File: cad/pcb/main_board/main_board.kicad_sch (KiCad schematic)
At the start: 0 parts

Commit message: VDDA, BOOT SEL
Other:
- sheet MCU ports: added ADC_IN[0..15]; removed none
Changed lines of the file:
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@@
       (effects (font (size 1.27 1.27)) (justify left top))
+    )
+    (pin "ADC_IN[0..15]" input (at 103.505 59.69 0)
+      (effects (font (size 1.27 1.27)) (justify right))
     )
     (instances

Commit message: HSE, usb, TC
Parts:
- added J1: USB_B_Micro, symbol Connector:USB_B_Micro
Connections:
- new net MCU/USB_D+: J1.3 (D+)
- new net MCU/USB_D-: J1.2 (D-)
- new net MCU/USB_ID: J1.4 (ID)
- new net VDD: J1.1 (VBUS)
- new net VSS: J1.5 (GND)
- no-connect marks 0 -> 1
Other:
- added sheet ThermoCouplePins (thermo_couple_pins.kicad_sch)
- sheet MCU ports: added USB_D+, USB_D-, USB_ID; removed none
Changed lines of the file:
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@@
 (kicad_sch (version 20230121) (generator eeschema)
   (paper "A4")
+  (no_connect (at 136.525 60.96))
+  (wire (pts (xy 103.505 66.04) (xy 126.365 66.04))
+    (stroke (width 0) (type default))
+  )
+  (bus (pts (xy 116.84 94.615) (xy 116.84 118.745))
+    (stroke (width 0) (type default))
+  )
+  (wire (pts (xy 103.505 68.58) (xy 126.365 68.58))
+    (stroke (width 0) (type default))
+  )
+  (bus (pts (xy 103.505 94.615) (xy 116.84 94.615))
+    (stroke (width 0) (type default))
+  )
+  (wire (pts (xy 120.65 76.2) (xy 126.365 76.2))
+    (stroke (width 0) (type default))
+  )
+  (wire (pts (xy 103.505 71.12) (xy 126.365 71.12))
+    (stroke (width 0) (type default))
+  )
+  (bus (pts (xy 116.84 118.745) (xy 104.14 118.745))
+    (stroke (width 0) (type default))
+  )
+  (wire (pts (xy 133.985 60.96) (xy 133.985 59.055))
+    (stroke (width 0) (type default))
+  )
+  (wire (pts (xy 120.015 59.055) (xy 133.985 59.055))
+    (stroke (width 0) (type default))
+  )
+  (global_label "VDD" (shape input) (at 120.65 76.2 180) (fields_autoplaced)
+    (effects (font (size 1.27 1.27)) (justify right))
+    (property "Intersheetrefs" "${INTERSHEET_REFS}" (at 114.0362 76.2 0)
+      (effects (font (size 1.27 1.27)) (justify right) hide)
+    )
+  )
+  (global_label "VSS" (shape input) (at 120.015 59.055 180) (fields_autoplaced)
+    (effects (font (size 1.27 1.27)) (justify right))
+    (property "Intersheetrefs" "${INTERSHEET_REFS}" (at 113.5222 59.055 0)
+      (effects (font (size 1.27 1.27)) (justify right) hide)
+    )
+  )
+  (symbol (lib_id "Connector:USB_B_Micro") (at 133.985 71.12 180) (unit 1)
+    (in_bom yes) (on_board yes) (dnp no) (fields_autoplaced)
+    (property "Reference" "J1" (at 140.97 69.85 0)
+      (effects (font (size 1.27 1.27)) (justify right))
+    )
+    (property "Value" "USB_B_Micro" (at 140.97 72.39 0)
+      (effects (font (size 1.27 1.27)) (justify right))
+    )
+    (property "Footprint" "" (at 130.175 69.85 0)
+      (effects (font (size 1.27 1.27)) hide)
+    )
+    (property "Datasheet" "~" (at 130.175 69.85 0)
+      (effects (font (size 1.27 1.27)) hide)
+    )
+    (pin "1")
+    (pin "2")
+    (pin "3")
+    (pin "4")
+    (pin "5")
+    (pin "6")
+    (instances
+      (project "main_board"
+        (path "/6c1b8035-64fa-4797-a506-5c9583cb241c"
+          (reference "J1") (unit 1)
+        )
+      )
+    )
+  )
   (sheet (at 30.48 55.245) (size 73.025 46.355) (fields_autoplaced)
     (stroke (width 0.1524) (type solid))
@@
       (effects (font (size 1.27 1.27)) (justify left top))
     )
-    (pin "ADC_IN[0..15]" input (at 103.505 59.69 0)
+    (pin "ADC_IN[0..15]" input (at 103.505 94.615 0)
+      (effects (font (size 1.27 1.27)) (justify right))
+    )
+    (pin "USB_D-" input (at 103.505 68.58 0)
+      (effects (font (size 1.27 1.27)) (justify right))
+    )
+    (pin "USB_D+" input (at 103.505 71.12 0)
+      (effects (font (size 1.27 1.27)) (justify right))
+    )
+    (pin "USB_ID" input (at 103.505 66.04 0)
       (effects (font (size 1.27 1.27)) (justify right))
     )
@@
       )
     )
+  )
+  (sheet (at 29.845 111.125) (size 74.295 37.465) (fields_autoplaced)
+    (stroke (width 0.1524) (type solid))
+    (fill (color 0 0 0 0.0000))
+    (property "Sheetname" "ThermoCouplePins" (at 29.845 110.4134 0)
+      (effects (font (size 1.27 1.27)) (justify left bottom))
+    )
+    (property "Sheetfile" "thermo_couple_pins.kicad_sch" (at 29.845 149.1746 0)
+      (effects (font (size 1.27 1.27)) (justify left top))
+    )
+    (pin "VOUT[0..15]" input (at 104.14 118.745 0)
+      (effects (font (size 1.27 1.27)) (justify right))
+    )
+    (instances
+      (project "main_board"
+        (path "/6c1b8035-64fa-4797-a506-5c9583cb241c" (page "4"))
+      )
+    )

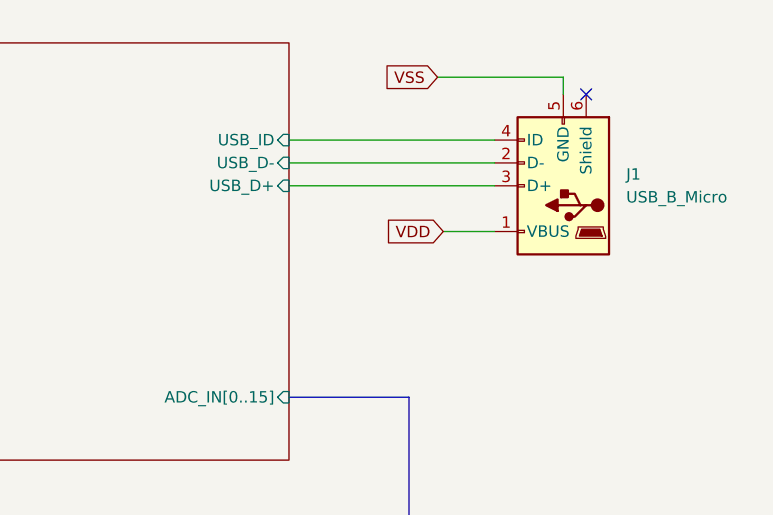
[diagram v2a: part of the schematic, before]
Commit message: Adding Voltage Regulators, Adding SD Card Symbol
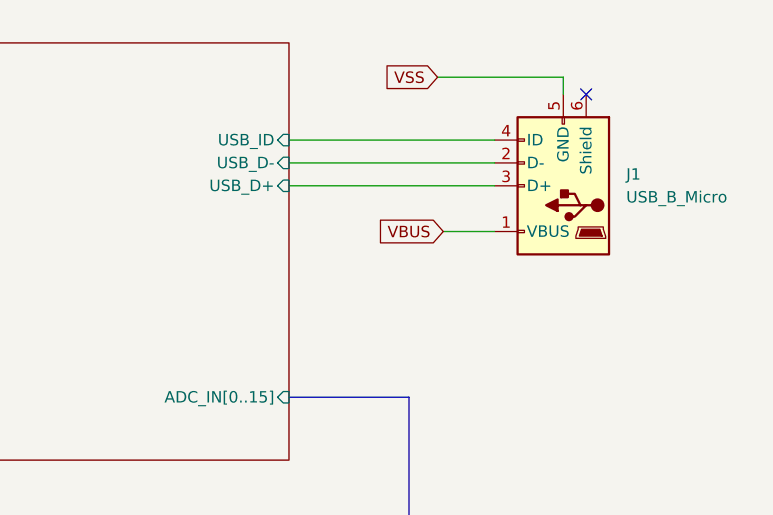
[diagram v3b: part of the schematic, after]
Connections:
- net VDD renamed VBUS
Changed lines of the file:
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@@
     (stroke (width 0) (type default))
   )
-  (global_label "VDD" (shape input) (at 120.65 76.2 180) (fields_autoplaced)
+  (global_label "VBUS" (shape input) (at 120.65 76.2 180) (fields_autoplaced)
     (effects (font (size 1.27 1.27)) (justify right))
-    (property "Intersheetrefs" "${INTERSHEET_REFS}" (at 114.0362 76.2 0)
+    (property "Intersheetrefs" "${INTERSHEET_REFS}" (at 112.7662 76.2 0)
       (effects (font (size 1.27 1.27)) (justify right) hide)
     )

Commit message: Add Aisler files
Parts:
- J1: footprint (none) -> Connector_USB:USB_Micro-B_Molex_47346-0001
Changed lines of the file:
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@@
       (effects (font (size 1.27 1.27)) (justify right))
     )
-    (property "Footprint" "" (at 130.175 69.85 0)
+    (property "Footprint" "Connector_USB:USB_Micro-B_Molex_47346-0001" (at 130.175 69.85 0)
       (effects (font (size 1.27 1.27)) hide)
     )

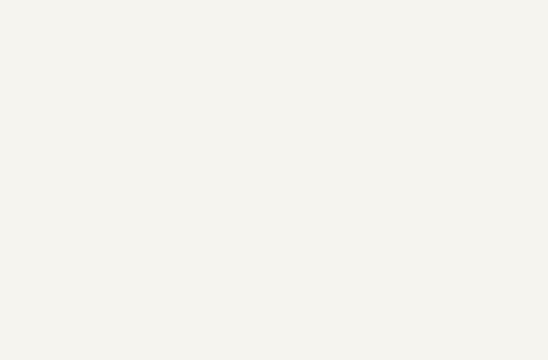
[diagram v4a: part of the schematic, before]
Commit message: First Layout of Voltage Regulator, Status LED note, add pulldown resistor for Voltage Regulator Enable
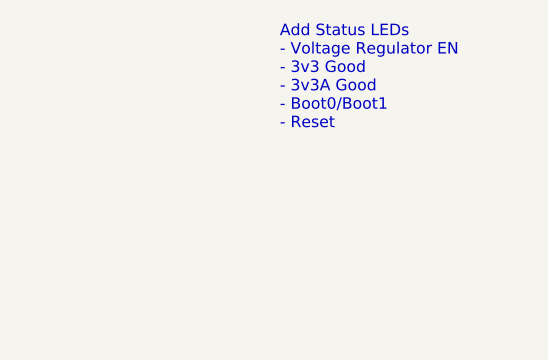
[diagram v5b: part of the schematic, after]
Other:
- note added: "Add Status LEDs - Voltage Regulator EN - 3v3 Good - 3v3A Good - Boot0/Boot1 - Reset"

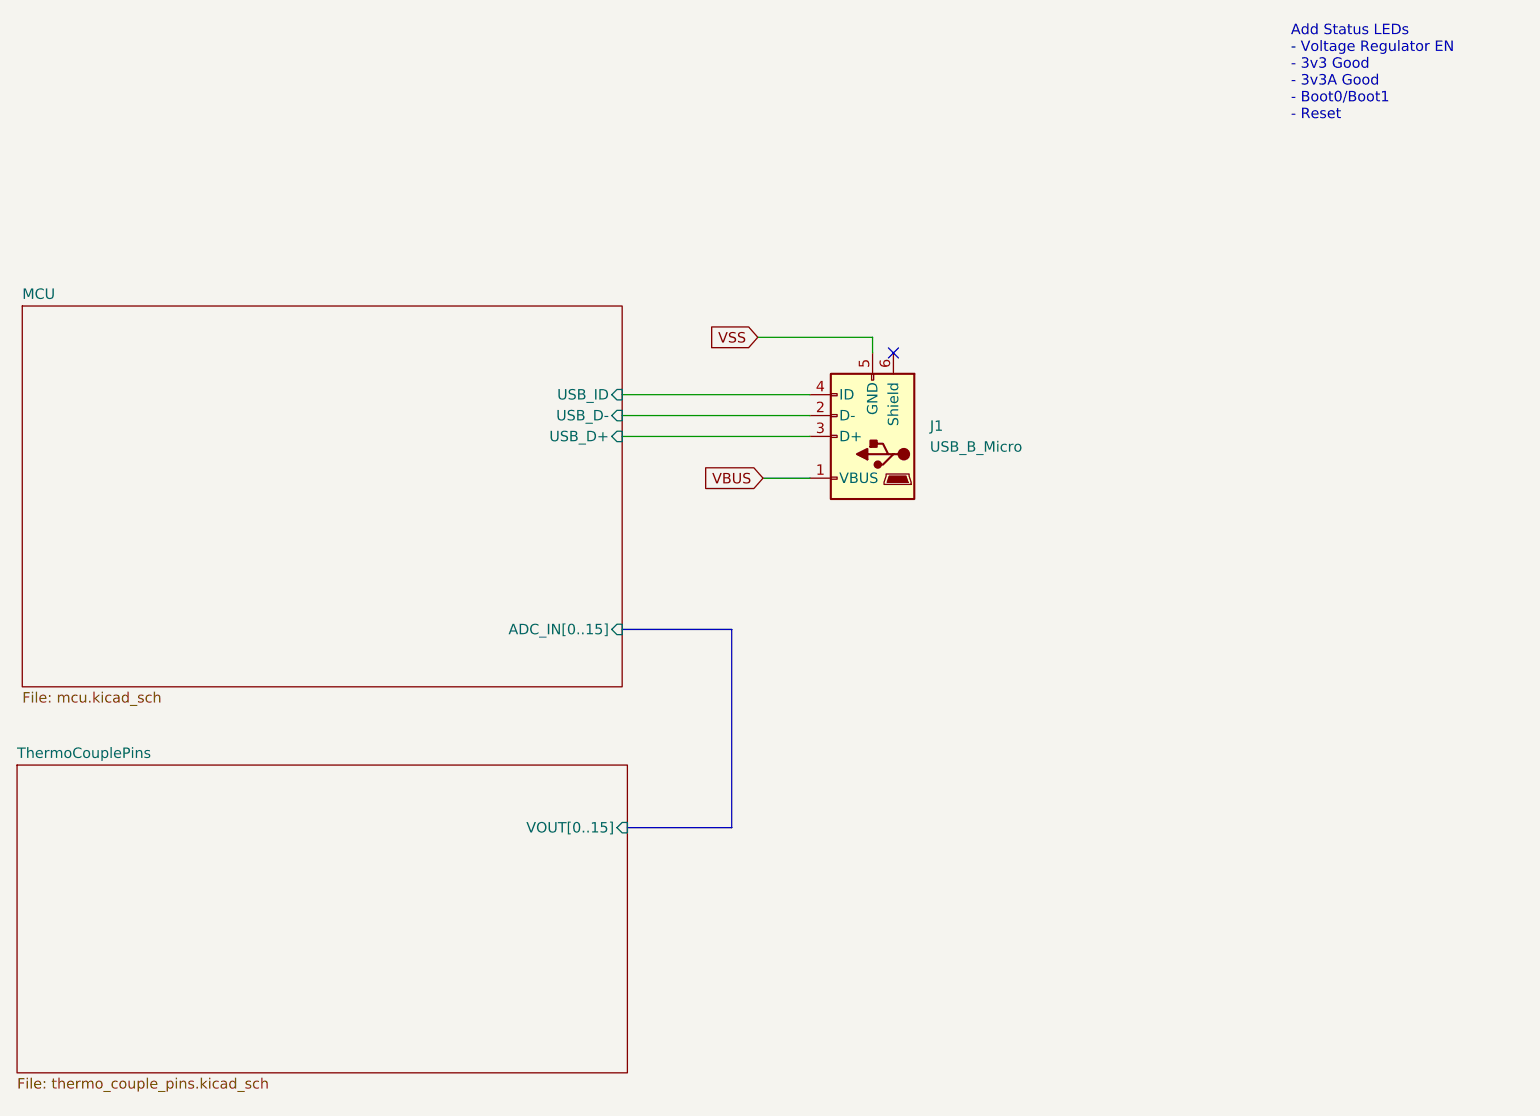
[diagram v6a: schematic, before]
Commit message: Adding JTAG Interface + POGO Pads
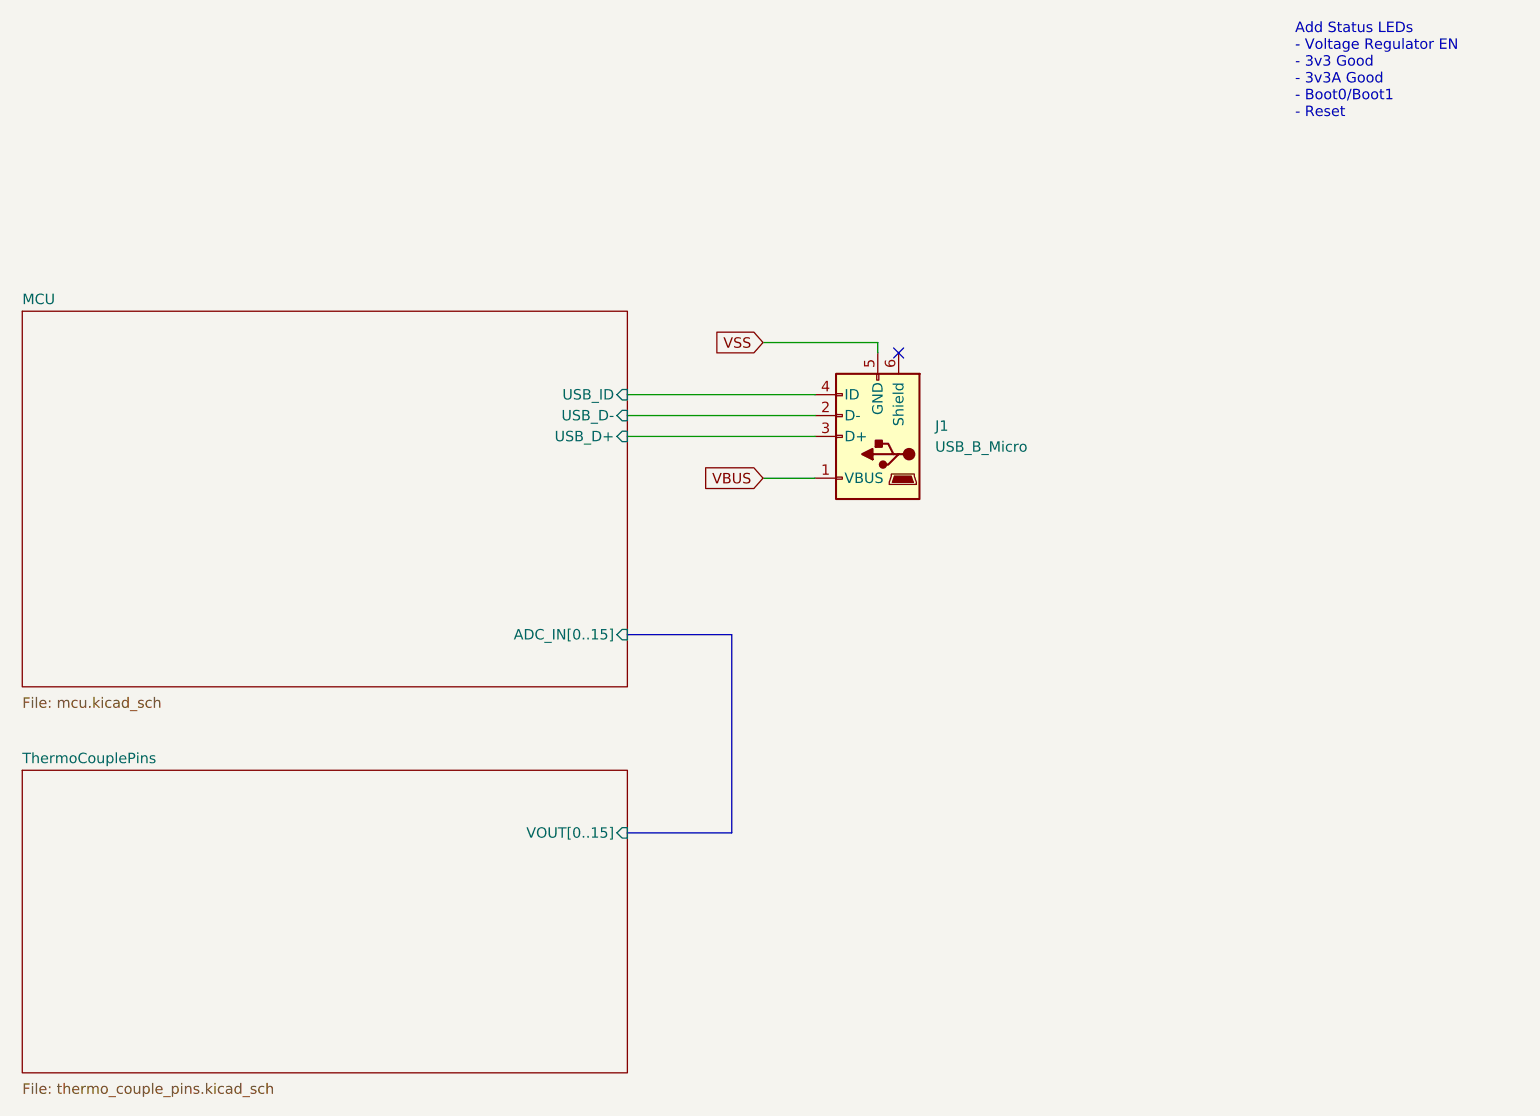
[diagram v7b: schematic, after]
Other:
- moved on the sheet: J1
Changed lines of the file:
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@@
 	(paper "A4")
 	(no_connect
-		(at 136.525 60.96)
-	)
-	(wire
-		(pts
-			(xy 103.505 66.04) (xy 126.365 66.04)
+		(at 137.16 60.96)
+	)
+	(wire
+		(pts
+			(xy 104.14 66.04) (xy 127 66.04)
 		)
 		(stroke
@@
 	(bus
 		(pts
-			(xy 116.84 94.615) (xy 116.84 118.745)
-		)
-		(stroke
-			(width 0)
-			(type default)
-		)
-	)
-	(wire
-		(pts
-			(xy 103.505 68.58) (xy 126.365 68.58)
+			(xy 116.84 95.25) (xy 116.84 119.38)
+		)
+		(stroke
+			(width 0)
+			(type default)
+		)
+	)
+	(wire
+		(pts
+			(xy 104.14 68.58) (xy 127 68.58)
 		)
 		(stroke
@@
 	(bus
 		(pts
-			(xy 103.505 94.615) (xy 116.84 94.615)
-		)
-		(stroke
-			(width 0)
-			(type default)
-		)
-	)
-	(wire
-		(pts
-			(xy 120.65 76.2) (xy 126.365 76.2)
-		)
-		(stroke
-			(width 0)
-			(type default)
-		)
-	)
-	(wire
-		(pts
-			(xy 103.505 71.12) (xy 126.365 71.12)
+			(xy 104.14 95.25) (xy 116.84 95.25)
+		)
+		(stroke
+			(width 0)
+			(type default)
+		)
+	)
+	(wire
+		(pts
+			(xy 120.65 76.2) (xy 127 76.2)
+		)
+		(stroke
+			(width 0)
+			(type default)
+		)
+	)
+	(wire
+		(pts
+			(xy 104.14 71.12) (xy 127 71.12)
 		)
 		(stroke
@@
 	(bus
 		(pts
-			(xy 116.84 118.745) (xy 104.14 118.745)
-		)
-		(stroke
-			(width 0)
-			(type default)
-		)
-	)
-	(wire
-		(pts
-			(xy 133.985 60.96) (xy 133.985 59.055)
-		)
-		(stroke
-			(width 0)
-			(type default)
-		)
-	)
-	(wire
-		(pts
-			(xy 120.015 59.055) (xy 133.985 59.055)
+			(xy 116.84 119.38) (xy 104.14 119.38)
+		)
+		(stroke
+			(width 0)
+			(type default)
+		)
+	)
+	(wire
+		(pts
+			(xy 134.62 60.96) (xy 134.62 59.69)
+		)
+		(stroke
+			(width 0)
+			(type default)
+		)
+	)
+	(wire
+		(pts
+			(xy 120.65 59.69) (xy 134.62 59.69)
 		)
 		(stroke
@@
 	(text "Add Status LEDs\n- Voltage Regulator EN\n- 3v3 Good\n- 3v3A Good\n- Boot0/Boot1\n- Reset"
 		(exclude_from_sim no)
-		(at 184.912 26.924 0)
+		(at 185.42 26.67 0)
 		(effects
 			(font
@@
 	(global_label "VSS"
 		(shape input)
-		(at 120.015 59.055 180)
+		(at 120.65 59.69 180)
 		(fields_autoplaced yes)
 		(effects
@@
 		)
 		(property "Intersheetrefs" "${INTERSHEET_REFS}"
-			(at 113.5222 59.055 0)
+			(at 114.1572 59.69 0)
 			(effects
 				(font
@@
 	(symbol
 		(lib_id "Connector:USB_B_Micro")
-		(at 133.985 71.12 180)
+		(at 134.62 71.12 180)
 		(unit 1)
 		(exclude_from_sim no)
@@
 		(fields_autoplaced yes)
 		(property "Reference" "J1"
-			(at 140.97 69.85 0)
+			(at 141.605 69.85 0)
 			(effects
 				(font
@@
 		)
 		(property "Value" "USB_B_Micro"
-			(at 140.97 72.39 0)
+			(at 141.605 72.39 0)
 			(effects
 				(font
@@
 		)
 		(property "Footprint" "Connector_USB:USB_Micro-B_Molex_47346-0001"
-			(at 130.175 69.85 0)
+			(at 130.81 69.85 0)
 			(effects
 				(font
@@
 		)
 		(property "Datasheet" "~"
-			(at 130.175 69.85 0)
-			(effects
-				(font
-					(size 1.27 1.27)
-				)
-				(hide yes)
-			)
-		)
-		(property "Description" ""
-			(at 133.985 71.12 0)
+			(at 130.81 69.85 0)
+			(effects
+				(font
+					(size 1.27 1.27)
+				)
+				(hide yes)
+			)
+		)
+		(property "Description" "USB Micro Type B connector"
+			(at 134.62 71.12 0)
 			(effects
 				(font
@@
 	)
 	(sheet
-		(at 30.48 55.245)
-		(size 73.025 46.355)
+		(at 30.48 55.88)
+		(size 73.66 45.72)
 		(fields_autoplaced yes)
 		(stroke
@@
 		)
 		(property "Sheetname" "MCU"
-			(at 30.48 54.5334 0)
+			(at 30.48 55.1684 0)
 			(effects
 				(font
@@
 		)
 		(property "Sheetfile" "mcu.kicad_sch"
-			(at 30.48 102.1846 0)
+			(at 30.48 102.8196 0)
 			(effects
 				(font
@@
 		)
 		(pin "ADC_IN[0..15]" input
-			(at 103.505 94.615 0)
+			(at 104.14 95.25 0)
 			(effects
 				(font
@@
 		)
 		(pin "USB_D-" input
-			(at 103.505 68.58 0)
+			(at 104.14 68.58 0)
 			(effects
 				(font
@@
 		)
 		(pin "USB_D+" input
-			(at 103.505 71.12 0)
+			(at 104.14 71.12 0)
 			(effects
 				(font
@@
 		)
 		(pin "USB_ID" input
-			(at 103.505 66.04 0)
+			(at 104.14 66.04 0)
 			(effects
 				(font
@@
 	)
 	(sheet
-		(at 29.845 111.125)
-		(size 74.295 37.465)
+		(at 30.48 111.76)
+		(size 73.66 36.83)
 		(fields_autoplaced yes)
 		(stroke
@@
 		)
 		(property "Sheetname" "ThermoCouplePins"
-			(at 29.845 110.4134 0)
+			(at 30.48 111.0484 0)
 			(effects
 				(font
@@
 		)
 		(property "Sheetfile" "thermo_couple_pins.kicad_sch"
-			(at 29.845 149.1746 0)
+			(at 30.48 149.8096 0)
 			(effects
 				(font
@@
 		)
 		(pin "VOUT[0..15]" input
-			(at 104.14 118.745 0)
-			(effects
-				(font
+			(at 104.14 119.38 0)
+			(effects
+				(font
